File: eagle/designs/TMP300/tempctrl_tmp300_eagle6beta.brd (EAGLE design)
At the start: 64 x 48 mm, 28 parts, among them IC1 TMP300, Q1 NIF5002

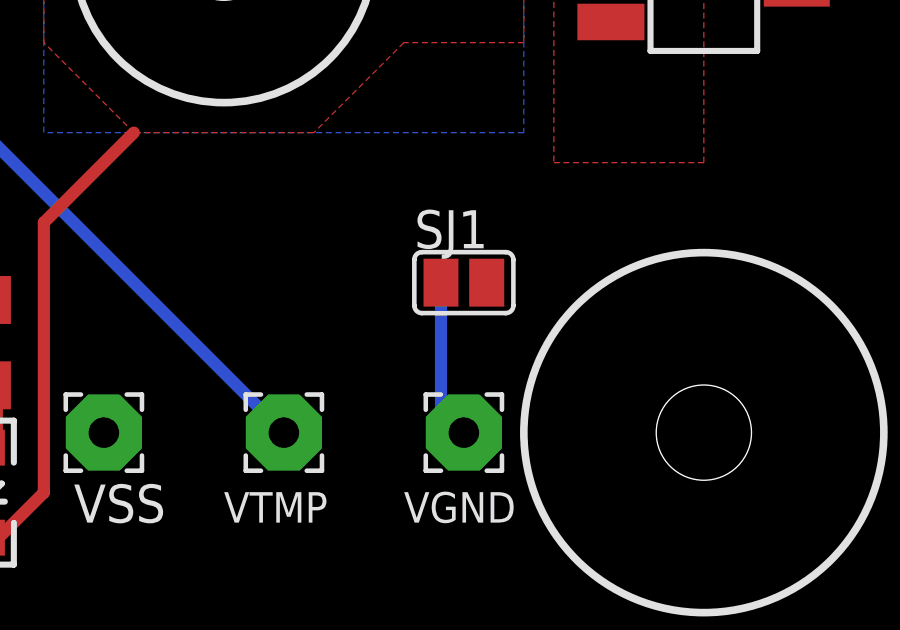
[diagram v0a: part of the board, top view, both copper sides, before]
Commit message: Manually added rot="R90" for component and ripped previous wire.
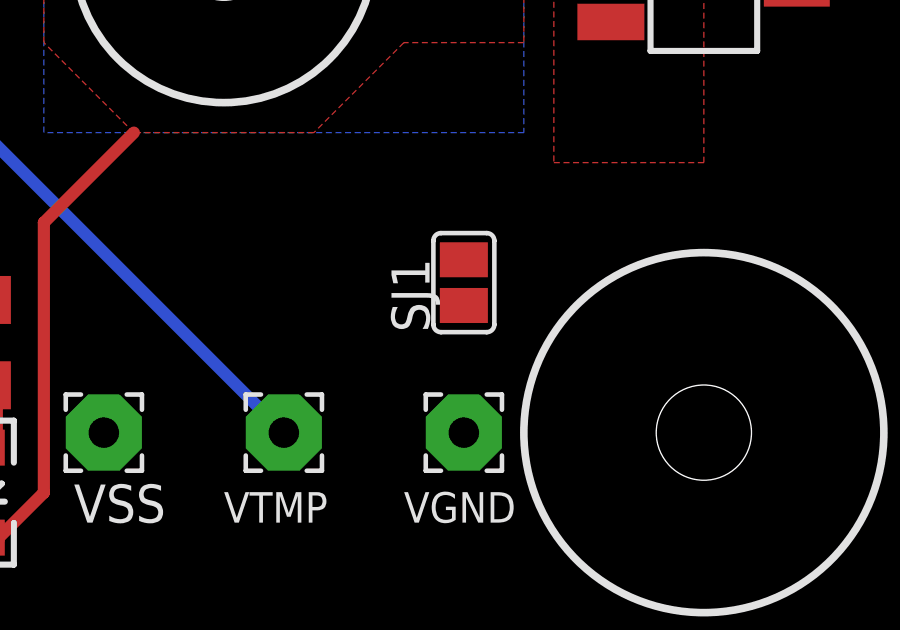
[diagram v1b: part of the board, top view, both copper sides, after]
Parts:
- turned SJ1 to 90 degrees
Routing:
- net N$1: track 5.32 -> 0.00 mm
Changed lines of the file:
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@@
 <element name="U$5" library="special-drill" package="DRILL_0.1250" value="" x="24" y="24"/>
 <element name="U$6" library="special-drill" package="DRILL_0.1250" value="" x="40" y="24"/>
-<element name="SJ1" library="jumper" package="SJ" value="" x="48" y="13"/>
+<element name="SJ1" library="jumper" package="SJ" value="" x="48" y="13" rot="R90"/>
 </elements>
 <signals>
@@
 </polygon>
 <contactref element="SJ1" pad="2"/>
-<wire x1="36" y1="8" x2="52.901" y2="21.689" width="0" layer="19" extent="1-1"/>
+<wire x1="48" y1="13.762" x2="52.901" y2="21.689" width="0" layer="19" extent="1-1"/>
+<wire x1="36" y1="8" x2="48" y2="13.762" width="0" layer="19" extent="1-1"/>
 <wire x1="22" y1="8" x2="36" y2="8" width="0" layer="19" extent="1-1"/>
-<wire x1="48.762" y1="13" x2="22" y2="8" width="0" layer="19" extent="1-1"/>
 <wire x1="10" y1="29.715" x2="22" y2="8" width="0" layer="19" extent="1-1"/>
 <wire x1="19.422" y1="34" x2="10" y2="29.715" width="0" layer="19" extent="1-1"/>
@@
 <contactref element="VGND" pad="1"/>
 <contactref element="SJ1" pad="1"/>
-<wire x1="48" y1="8" x2="47.238" y2="8.762" width="0.4064" layer="16"/>
-<wire x1="47.238" y1="8.762" x2="47.238" y2="13" width="0.4064" layer="16"/>
+<wire x1="48" y1="8" x2="47.238" y2="8.762" width="0" layer="19" extent="1-16"/>
+<wire x1="47.238" y1="8.762" x2="47.238" y2="13" width="0" layer="19" extent="1-16"/>
 <wire x1="47.238" y1="13" x2="47.238" y2="13" width="0" layer="19" extent="1-16"/>
 </signal>

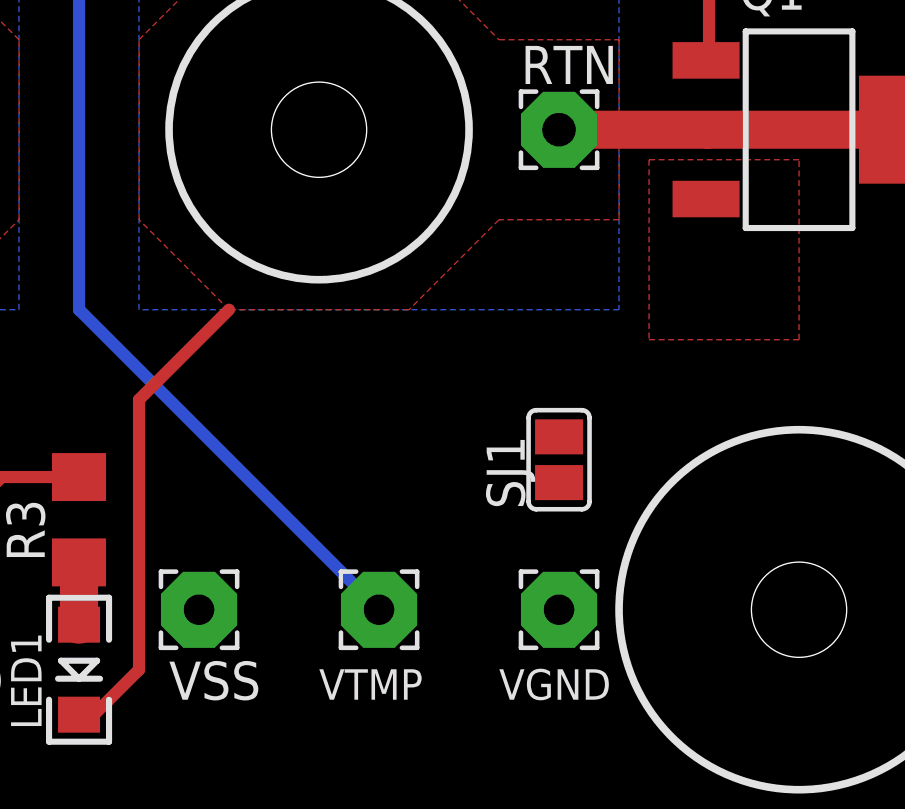
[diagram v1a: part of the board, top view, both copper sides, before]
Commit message: Finished up routing.
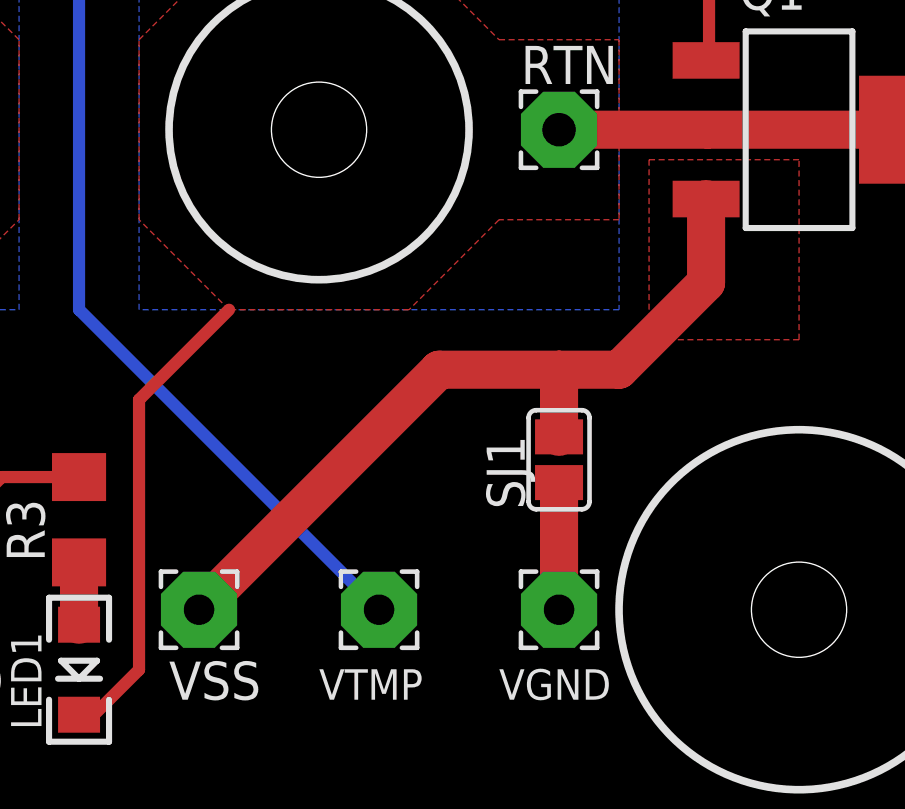
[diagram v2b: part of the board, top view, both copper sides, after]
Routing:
- net GND: track 5.04 -> 31.5 mm
- net N$1: track 0.00 -> 4.00 mm
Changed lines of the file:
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@@
 </polygon>
 <contactref element="SJ1" pad="2"/>
-<wire x1="48" y1="13.762" x2="52.901" y2="21.689" width="0" layer="19" extent="1-1"/>
-<wire x1="36" y1="8" x2="48" y2="13.762" width="0" layer="19" extent="1-1"/>
-<wire x1="22" y1="8" x2="36" y2="8" width="0" layer="19" extent="1-1"/>
-<wire x1="10" y1="29.715" x2="22" y2="8" width="0" layer="19" extent="1-1"/>
-<wire x1="19.422" y1="34" x2="10" y2="29.715" width="0" layer="19" extent="1-1"/>
-<wire x1="33.254" y1="39.286" x2="22.6" y2="34" width="0" layer="19" extent="1-1"/>
+<wire x1="36" y1="8" x2="44" y2="16" width="1.27" layer="1"/>
+<wire x1="44" y1="16" x2="48" y2="16" width="1.27" layer="1"/>
+<wire x1="48" y1="16" x2="50" y2="16" width="1.27" layer="1"/>
+<wire x1="50" y1="16" x2="52.901" y2="18.901" width="1.27" layer="1"/>
+<wire x1="52.901" y1="18.901" x2="52.901" y2="21.689" width="1.27" layer="1"/>
+<wire x1="48" y1="13.762" x2="48" y2="16" width="1.27" layer="1"/>
 </signal>
 <signal name="N$4">
@@
 <contactref element="VGND" pad="1"/>
 <contactref element="SJ1" pad="1"/>
-<wire x1="48" y1="8" x2="47.238" y2="8.762" width="0" layer="19" extent="1-16"/>
-<wire x1="47.238" y1="8.762" x2="47.238" y2="13" width="0" layer="19" extent="1-16"/>
-<wire x1="47.238" y1="13" x2="47.238" y2="13" width="0" layer="19" extent="1-16"/>
+<wire x1="48" y1="8" x2="48" y2="12" width="1.27" layer="1"/>
+<wire x1="48" y1="12" x2="48" y2="12.238" width="0" layer="19" extent="1-1"/>
 </signal>
 </signals>
